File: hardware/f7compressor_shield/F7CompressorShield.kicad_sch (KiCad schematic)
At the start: 12 parts, among them CN10 NUCLEO Zio CN10 (17x2), CN7 NUCLEO Zio CN7 (10x2), CN8 NUCLEO Zio CN8 (8x2), CN9 NUCLEO Zio CN9 (15x2), J1 LCD P1/P2 (ILI9341+XPT2046), J2 Relay module J1 (VCC/GND/IN1-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, J3 OIL_SW field terminal, J4 ESTOP field terminal, J5 4-20mA pressure loop field te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, U1 NUCLEO-H723ZG Morpho (CN11/CN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

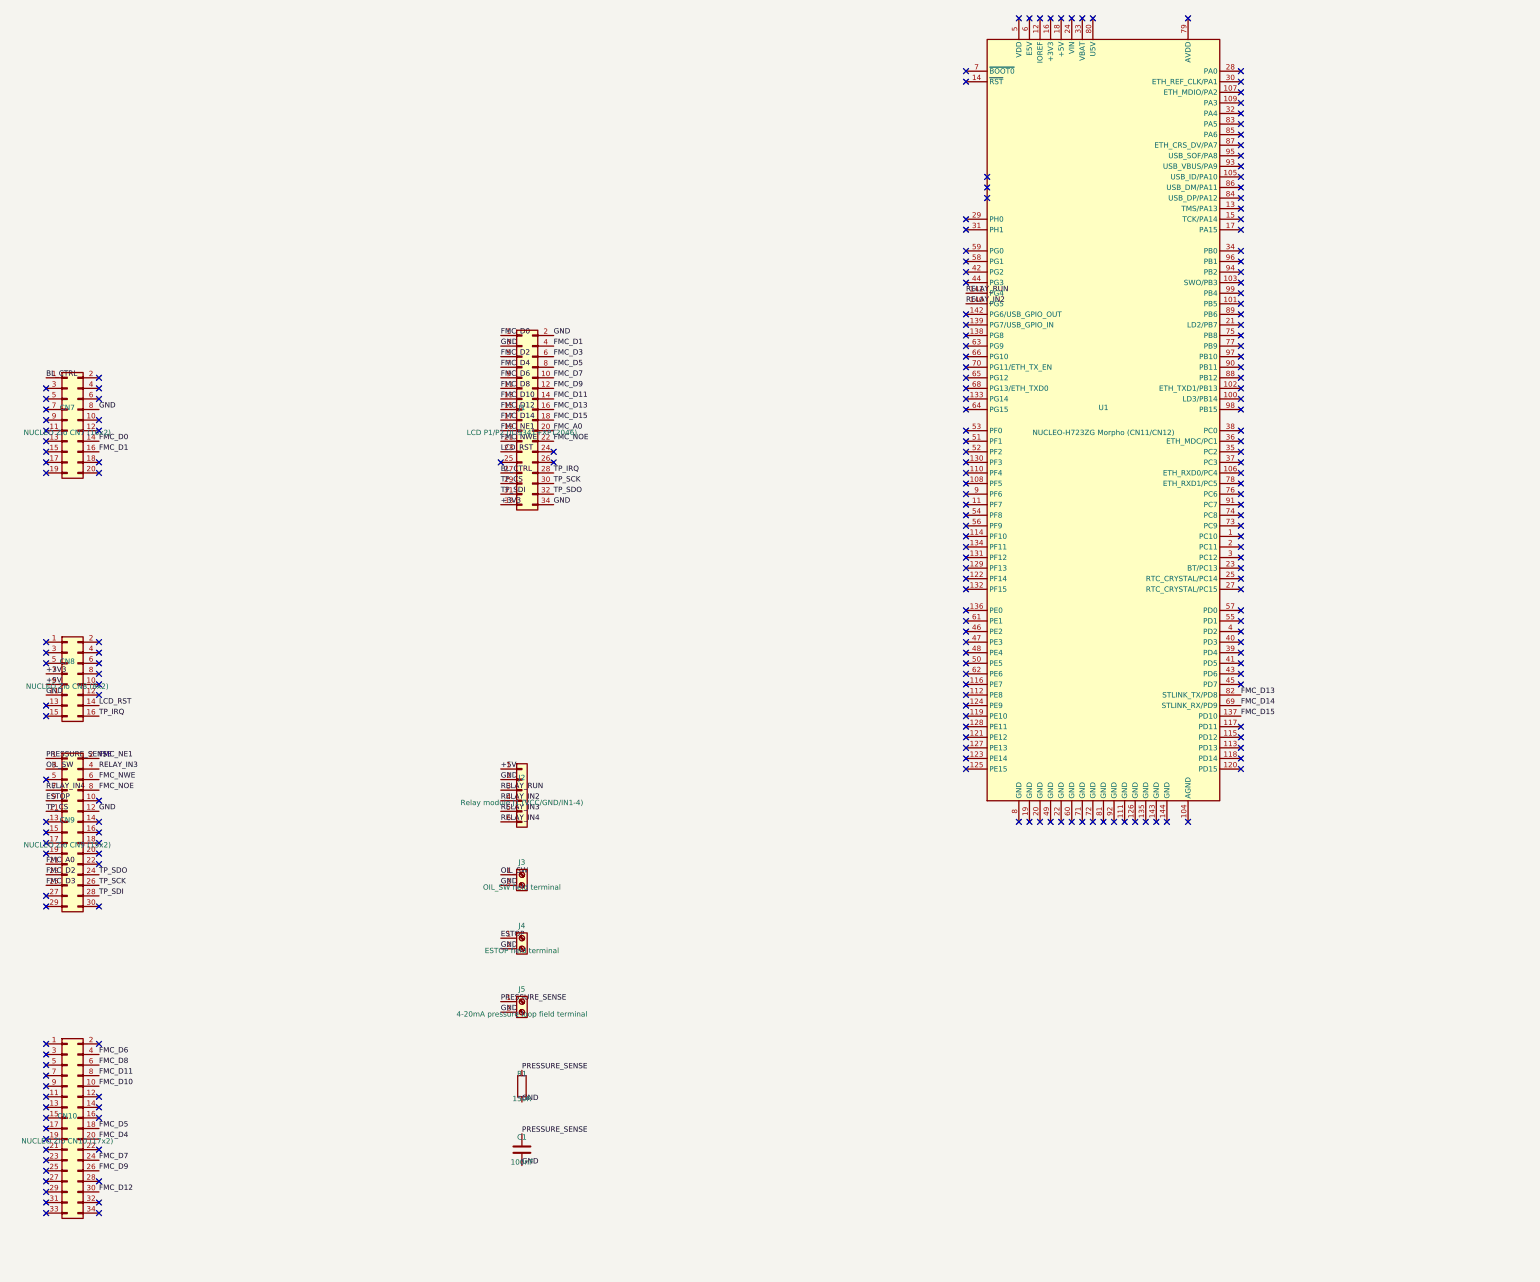
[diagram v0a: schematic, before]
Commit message: Fix Zio/LCD header pin-1 orientation on shield PCB; re-route
Pin 1's physical column (and its square silkscreen marker) didn't match
the real Nucleo/LCD silkscreen on CN7-CN10 and J1 -- the generic KiCad
Odd_Even footprint's pad 1/2 assignment is mirrored relative to the real
boards. Fixed by mirroring the footprints themselves (not swapping net
assignments, which is electrically equivalent but leaves the pin-1
marker in the wrong physical spot). Also fixed 3 clearance violations
left by the re-route and confirmed CN12/FMC pin alternate-function
questions against the Nucleo schematic and MCU datasheet -- no other
conflicts beyond the already-documented PD8/PD9 VCP/FMC_D13-D14 reuse.

ERC clean, DRC 0 unconnected items, same expected-findings baseline.

Co-Authored-By: Claude Sonnet 5 <noreply@anthropic.com>
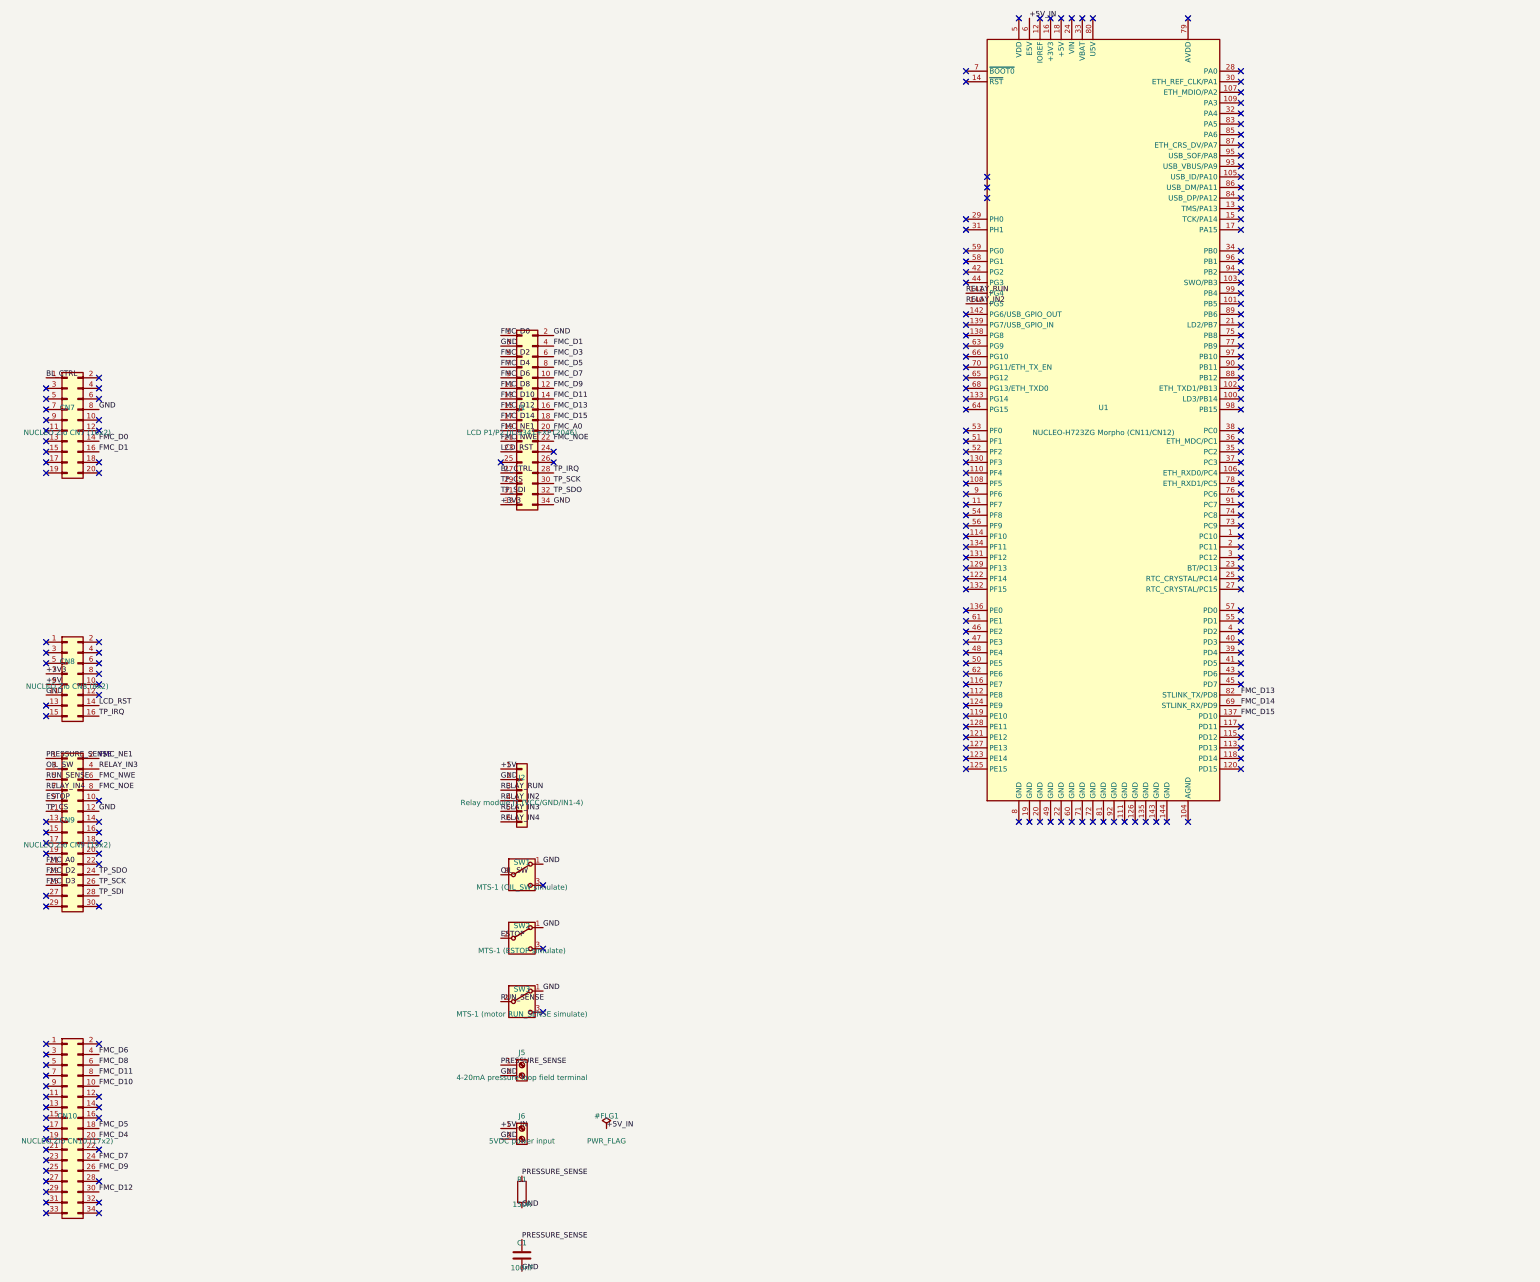
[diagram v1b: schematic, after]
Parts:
- removed J3: OIL_SW field terminal, TerminalBlock:TerminalBlock_MaiXu_MX126-5.0-02P_1x02_P5.00mm, symbol Connector:Screw_Terminal_01x02
- removed J4: ESTOP field terminal, TerminalBlock:TerminalBlock_MaiXu_MX126-5.0-02P_1x02_P5.00mm, symbol Connector:Screw_Terminal_01x02
- added J6: 5VDC power input, TerminalBlock:TerminalBlock_MaiXu_MX126-5.0-02P_1x02_P5.00mm, symbol Connector:Screw_Terminal_01x02
- added SW1: MTS-1 (OIL_SW simulate), MTS-1:SW_MTS-1, symbol Switch:SW_SPDT
- added SW2: MTS-1 (ESTOP simulate), MTS-1:SW_MTS-1, symbol Switch:SW_SPDT
- added SW3: MTS-1 (motor RUN_SENSE simulate), MTS-1:SW_MTS-1, symbol Switch:SW_SPDT
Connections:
- net ESTOP: now also SW2.2 (B)
- net GND: now also J6.2 (Pin_2), SW1.1 (A), SW2.1 (A), SW3.1 (A)
- net OIL_SW: now also SW1.2 (B)
- net RUN_SENSE: now reaches CN9.5 (Pin_5)
- net RUN_SENSE: now also SW3.2 (B)
- net +5V_IN: now reaches U1.6 (E5V)
- net +5V_IN: now also J6.1 (Pin_1)
- no-connect marks 208 -> 209
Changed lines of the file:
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@@
 	)
 	(symbol
-		(lib_id "Connector:Screw_Terminal_01x02")
+		(lib_id "Switch:SW_SPDT")
 		(at 259.08 109.22 0)
 		(unit 1)
@@
 		(on_board yes)
 		(dnp no)
-		(property "Reference" "J3"
+		(property "Reference" "SW1"
 			(at 259.08 106.22 0)
 			(effects (font (size 1.27 1.27)))
 		)
-		(property "Value" "OIL_SW field terminal"
+		(property "Value" "MTS-1 (OIL_SW simulate)"
 			(at 259.08 112.22 0)
 			(effects (font (size 1.27 1.27)))
 		)
-		(property "Footprint" "TerminalBlock:TerminalBlock_MaiXu_MX126-5.0-02P_1x02_P5.00mm"
+		(property "Footprint" "MTS-1:SW_MTS-1"
 			(at 259.08 109.22 0)
 			(effects (font (size 1.27 1.27)) (hide yes))
@@
 		)
 		(pin "2"
+		)
+		(pin "3"
 		)
 		(instances
 			(project "F7CompressorShield"
 				(path "/11111111-1111-1111-1111-111111111111"
-					(reference "J3")
+					(reference "SW1")
 					(unit 1)
 				)
@@
 	)
 	(symbol
-		(lib_id "Connector:Screw_Terminal_01x02")
+		(lib_id "Switch:SW_SPDT")
 		(at 259.08 124.46 0)
 		(unit 1)
@@
 		(on_board yes)
 		(dnp no)
-		(property "Reference" "J4"
+		(property "Reference" "SW2"
 			(at 259.08 121.46 0)
 			(effects (font (size 1.27 1.27)))
 		)
-		(property "Value" "ESTOP field terminal"
+		(property "Value" "MTS-1 (ESTOP simulate)"
 			(at 259.08 127.46 0)
 			(effects (font (size 1.27 1.27)))
 		)
-		(property "Footprint" "TerminalBlock:TerminalBlock_MaiXu_MX126-5.0-02P_1x02_P5.00mm"
+		(property "Footprint" "MTS-1:SW_MTS-1"
 			(at 259.08 124.46 0)
 			(effects (font (size 1.27 1.27)) (hide yes))
@@
 		)
 		(pin "2"
+		)
+		(pin "3"
 		)
 		(instances
 			(project "F7CompressorShield"
 				(path "/11111111-1111-1111-1111-111111111111"
-					(reference "J4")
+					(reference "SW2")
 					(unit 1)
 				)
@@
 	)
 	(symbol
-		(lib_id "Connector:Screw_Terminal_01x02")
+		(lib_id "Switch:SW_SPDT")
 		(at 259.08 139.7 0)
 		(unit 1)
@@
 		(on_board yes)
 		(dnp no)
+		(property "Reference" "SW3"
+			(at 259.08 136.7 0)
+			(effects (font (size 1.27 1.27)))
+		)
+		(property "Value" "MTS-1 (motor RUN_SENSE simulate)"
+			(at 259.08 142.7 0)
+			(effects (font (size 1.27 1.27)))
+		)
+		(property "Footprint" "MTS-1:SW_MTS-1"
+			(at 259.08 139.7 0)
+			(effects (font (size 1.27 1.27)) (hide yes))
+		)
+		(pin "1"
+		)
+		(pin "2"
+		)
+		(pin "3"
+		)
+		(instances
+			(project "F7CompressorShield"
+				(path "/11111111-1111-1111-1111-111111111111"
+					(reference "SW3")
+					(unit 1)
+				)
+			)
+		)
+	)
+	(symbol
+		(lib_id "Connector:Screw_Terminal_01x02")
+		(at 259.08 154.94 0)
+		(unit 1)
+		(exclude_from_sim no)
+		(in_bom yes)
+		(on_board yes)
+		(dnp no)
 		(property "Reference" "J5"
-			(at 259.08 136.7 0)
+			(at 259.08 151.94 0)
 			(effects (font (size 1.27 1.27)))
 		)
 		(property "Value" "4-20mA pressure loop field terminal"
-			(at 259.08 142.7 0)
+			(at 259.08 157.94 0)
 			(effects (font (size 1.27 1.27)))
 		)
 		(property "Footprint" "TerminalBlock:TerminalBlock_MaiXu_MX126-5.0-02P_1x02_P5.00mm"
-			(at 259.08 139.7 0)
+			(at 259.08 154.94 0)
 			(effects (font (size 1.27 1.27)) (hide yes))
 		)
@@
 	)
 	(symbol
+		(lib_id "Connector:Screw_Terminal_01x02")
+		(at 259.08 170.18 0)
+		(unit 1)
+		(exclude_from_sim no)
+		(in_bom yes)
+		(on_board yes)
+		(dnp no)
+		(property "Reference" "J6"
+			(at 259.08 167.18 0)
+			(effects (font (size 1.27 1.27)))
+		)
+		(property "Value" "5VDC power input"
+			(at 259.08 173.18 0)
+			(effects (font (size 1.27 1.27)))
+		)
+		(property "Footprint" "TerminalBlock:TerminalBlock_MaiXu_MX126-5.0-02P_1x02_P5.00mm"
+			(at 259.08 170.18 0)
+			(effects (font (size 1.27 1.27)) (hide yes))
+		)
+		(pin "1"
+		)
+		(pin "2"
+		)
+		(instances
+			(project "F7CompressorShield"
+				(path "/11111111-1111-1111-1111-111111111111"
+					(reference "J6")
+					(unit 1)
+				)
+			)
+		)
+	)
+	(symbol
+		(lib_id "power:PWR_FLAG")
+		(at 279.4 170.18 0)
+		(unit 1)
+		(exclude_from_sim no)
+		(in_bom yes)
+		(on_board yes)
+		(dnp no)
+		(property "Reference" "#FLG1"
+			(at 279.4 167.18 0)
+			(effects (font (size 1.27 1.27)))
+		)
+		(property "Value" "PWR_FLAG"
+			(at 279.4 173.18 0)
+			(effects (font (size 1.27 1.27)))
+		)
+		(property "Footprint" ""
+			(at 279.4 170.18 0)
+			(effects (font (size 1.27 1.27)) (hide yes))
+		)
+		(pin "1"
+		)
+		(instances
+			(project "F7CompressorShield"
+				(path "/11111111-1111-1111-1111-111111111111"
+					(reference "#FLG1")
+					(unit 1)
+				)
+			)
+		)
+	)
+	(symbol
 		(lib_id "Device:R")
-		(at 259.08 160.02 0)
+		(at 259.08 185.42 0)
 		(unit 1)
 		(exclude_from_sim no)
@@
 		(dnp no)
 		(property "Reference" "R1"
-			(at 259.08 157.02 0)
+			(at 259.08 182.42 0)
 			(effects (font (size 1.27 1.27)))
 		)
 		(property "Value" "150R"
-			(at 259.08 163.02 0)
+			(at 259.08 188.42 0)
 			(effects (font (size 1.27 1.27)))
 		)
 		(property "Footprint" "Resistor_THT:R_Axial_DIN0207_L6.3mm_D2.5mm_P10.16mm_Horizontal"
-			(at 259.08 160.02 0)
+			(at 259.08 185.42 0)
 			(effects (font (size 1.27 1.27)) (hide yes))
 		)
@@
 	(symbol
 		(lib_id "Device:C")
-		(at 259.08 175.26 0)
+		(at 259.08 200.66 0)
 		(unit 1)
 		(exclude_from_sim no)
@@
 		(dnp no)
 		(property "Reference" "C1"
-			(at 259.08 172.26 0)
+			(at 259.08 197.66 0)
 			(effects (font (size 1.27 1.27)))
 		)
 		(property "Value" "100nF"
-			(at 259.08 178.26 0)
+			(at 259.08 203.66 0)
 			(effects (font (size 1.27 1.27)))
 		)
 		(property "Footprint" "Capacitor_THT:C_Disc_D3.0mm_W1.6mm_P2.50mm"
-			(at 259.08 175.26 0)
+			(at 259.08 200.66 0)
 			(effects (font (size 1.27 1.27)) (hide yes))
 		)
@@
 		(effects (font (size 1.27 1.27)) (justify left bottom))
 	)
+	(label "RUN_SENSE"
+		(at 144.78 86.36 0)
+		(effects (font (size 1.27 1.27)) (justify left bottom))
+	)
 	(label "FMC_NWE"
 		(at 157.48 86.36 0)
@@
 		(effects (font (size 1.27 1.27)) (justify left bottom))
 	)
+	(label "+5V_IN"
+		(at 381 -96.52 0)
+		(effects (font (size 1.27 1.27)) (justify left bottom))
+	)
 	(label "FMC_D0"
 		(at 254 -20.32 0)
@@
 	)
 	(label "GND"
-		(at 254 111.76 0)
+		(at 264.16 106.68 0)
 		(effects (font (size 1.27 1.27)) (justify left bottom))
 	)
@@
 	)
 	(label "GND"
-		(at 254 127 0)
+		(at 264.16 121.92 0)
+		(effects (font (size 1.27 1.27)) (justify left bottom))
+	)
+	(label "RUN_SENSE"
+		(at 254 139.7 0)
+		(effects (font (size 1.27 1.27)) (justify left bottom))
+	)
+	(label "GND"
+		(at 264.16 137.16 0)
 		(effects (font (size 1.27 1.27)) (justify left bottom))
 	)
 	(label "PRESSURE_SENSE"
-		(at 254 139.7 0)
-		(effects (font (size 1.27 1.27)) (justify left bottom))
-	)
-	(label "GND"
-		(at 254 142.24 0)
+		(at 254 154.94 0)
+		(effects (font (size 1.27 1.27)) (justify left bottom))
+	)
+	(label "GND"
+		(at 254 157.48 0)
+		(effects (font (size 1.27 1.27)) (justify left bottom))
+	)
+	(label "+5V_IN"
+		(at 254 170.18 0)
+		(effects (font (size 1.27 1.27)) (justify left bottom))
+	)
+	(label "GND"
+		(at 254 172.72 0)
+		(effects (font (size 1.27 1.27)) (justify left bottom))
+	)
+	(label "+5V_IN"
+		(at 279.4 170.18 0)
 		(effects (font (size 1.27 1.27)) (justify left bottom))
 	)
 	(label "PRESSURE_SENSE"
-		(at 259.08 156.21 0)
-		(effects (font (size 1.27 1.27)) (justify left bottom))
-	)
-	(label "GND"
-		(at 259.08 163.83 0)
+		(at 259.08 181.61 0)
+		(effects (font (size 1.27 1.27)) (justify left bottom))
+	)
+	(label "GND"
+		(at 259.08 189.23 0)
 		(effects (font (size 1.27 1.27)) (justify left bottom))
 	)
 	(label "PRESSURE_SENSE"
-		(at 259.08 171.45 0)
-		(effects (font (size 1.27 1.27)) (justify left bottom))
-	)
-	(label "GND"
-		(at 259.08 179.07 0)
+		(at 259.08 196.85 0)
+		(effects (font (size 1.27 1.27)) (justify left bottom))
+	)
+	(label "GND"
+		(at 259.08 204.47 0)
 		(effects (font (size 1.27 1.27)) (justify left bottom))
 	)
@@
 	)
 	(no_connect
-		(at 144.78 86.36)
-	)
-	(no_connect
 		(at 157.48 91.44)
 	)
@@
 	)
 	(no_connect
-		(at 381 -96.52)
-	)
-	(no_connect
 		(at 365.76 -83.82)
 	)
@@
 		(at 266.7 10.16)
 	)
+	(no_connect
+		(at 264.16 111.76)
+	)
+	(no_connect
+		(at 264.16 127)
+	)
+	(no_connect
+		(at 264.16 142.24)
+	)
 	(sheet_instances
